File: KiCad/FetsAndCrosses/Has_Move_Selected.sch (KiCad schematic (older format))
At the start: 0 parts

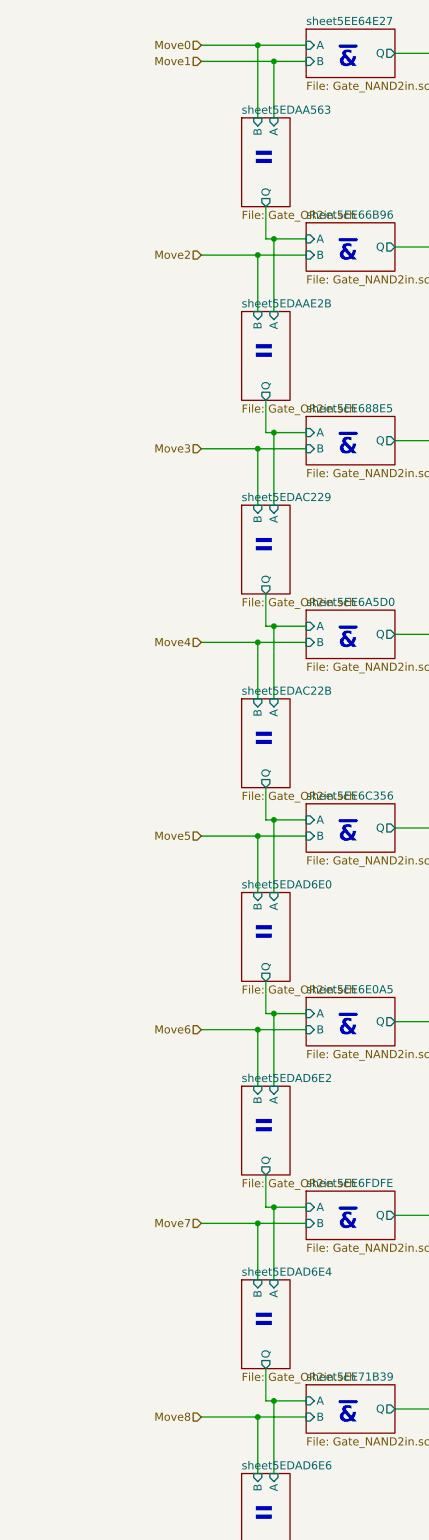
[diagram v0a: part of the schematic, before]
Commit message: Reworked everything to use Buses
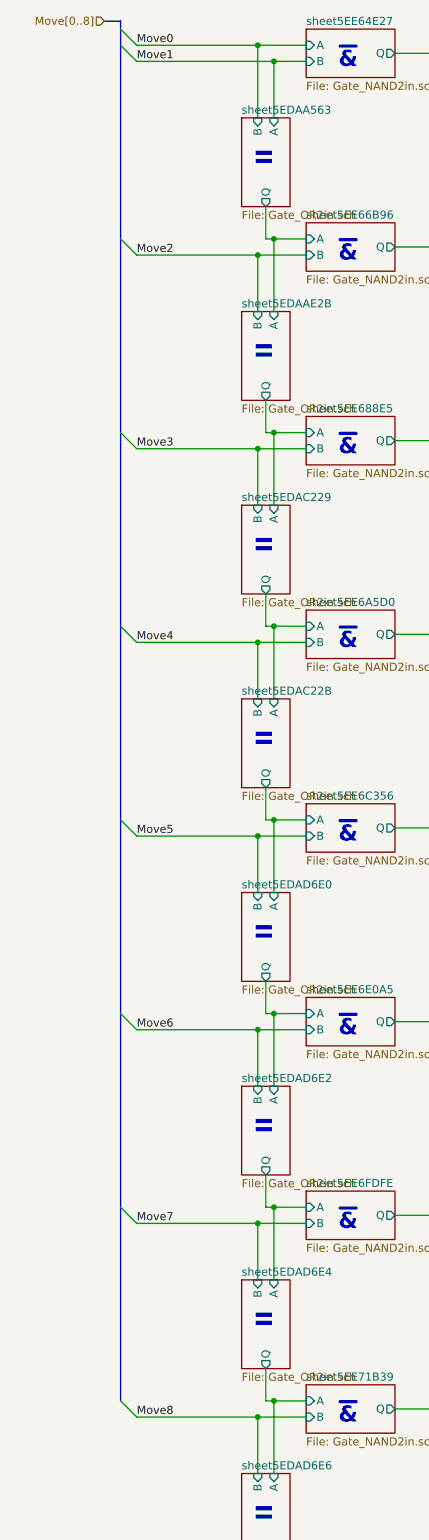
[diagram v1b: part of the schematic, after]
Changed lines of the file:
@@
 $Descr A4 8268 11693 portrait
 encoding utf-8
-Sheet 67 215
+Sheet 176 400
 Title ""
 Date ""
@@
 Comment4 ""
 $EndDescr
-Text HLabel 1700 800  0    50   Input ~ 0
-Move0
 Text Notes 2150 1450 3    100  ~ 20
 II
@@
 Wire Wire Line
 	2050 9300 2350 9300
-Wire Wire Line
-	2150 900  1700 900
 Connection ~ 2150 900
-Wire Wire Line
-	2050 800  1700 800
 Connection ~ 2050 800
-Wire Wire Line
-	1700 2100 2050 2100
-Wire Wire Line
-	1700 3300 2050 3300
-Wire Wire Line
-	1700 4500 2050 4500
-Wire Wire Line
-	1700 5700 2050 5700
-Wire Wire Line
-	1700 6900 2050 6900
-Wire Wire Line
-	1700 8100 2050 8100
-Wire Wire Line
-	1700 9300 2050 9300
-Text HLabel 1700 9300 0    50   Input ~ 0
-Move8
-Text HLabel 1700 8100 0    50   Input ~ 0
-Move7
-Text HLabel 1700 6900 0    50   Input ~ 0
-Move6
-Text HLabel 1700 5700 0    50   Input ~ 0
-Move5
-Text HLabel 1700 4500 0    50   Input ~ 0
-Move4
-Text HLabel 1700 3300 0    50   Input ~ 0
-Move3
-Text HLabel 1700 2100 0    50   Input ~ 0
-Move2
-Text HLabel 1700 900  0    50   Input ~ 0
-Move1
 $Sheet
 S 5550 1950 550  300
@@
 Text Notes 4700 2150 0    100  ~ 20
 &
+Entry Wire Line
+	1200 700  1300 800
+Entry Wire Line
+	1200 800  1300 900
+Entry Wire Line
+	1200 2000 1300 2100
+Entry Wire Line
+	1200 4400 1300 4500
+Entry Wire Line
+	1200 5600 1300 5700
+Entry Wire Line
+	1200 6800 1300 6900
+Entry Wire Line
+	1200 8000 1300 8100
+Entry Wire Line
+	1200 9200 1300 9300
+Wire Bus Line
+	1200 650  1100 650
+Text HLabel 1100 650  0    50   Input ~ 0
+Move[0..8]
+Text Label 1300 800  0    50   ~ 0
+Move0
+Text Label 1300 900  0    50   ~ 0
+Move1
+Text Label 1300 2100 0    50   ~ 0
+Move2
+Text Label 1300 4500 0    50   ~ 0
+Move4
+Text Label 1300 5700 0    50   ~ 0
+Move5
+Text Label 1300 6900 0    50   ~ 0
+Move6
+Text Label 1300 8100 0    50   ~ 0
+Move7
+Text Label 1300 9300 0    50   ~ 0
+Move8
+Text Label 1300 3300 0    50   ~ 0
+Move3
+Entry Wire Line
+	1200 3200 1300 3300
+Wire Wire Line
+	1300 9300 2050 9300
+Wire Wire Line
+	1300 8100 2050 8100
+Wire Wire Line
+	1300 6900 2050 6900
+Wire Wire Line
+	1300 5700 2050 5700
+Wire Wire Line
+	1300 4500 2050 4500
+Wire Wire Line
+	1300 3300 2050 3300
+Wire Wire Line
+	1300 2100 2050 2100
+Wire Wire Line
+	1300 800  2050 800
+Wire Wire Line
+	1300 900  2150 900
+Wire Bus Line
+	1200 650  1200 9200
 $EndSCHEMATC

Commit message: Schematic fixes.
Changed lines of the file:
@@
 Sheet 223 389
 Title ""
-Date ""
-Rev ""
-Comp ""
-Comment1 ""
+Date "2020-07-05"
+Rev "v0.0"
+Comp "Philipp Schilk"
+Comment1 "c"
 Comment2 ""
 Comment3 ""
@@
 Wire Wire Line
 	1300 900  2150 900
-Wire Bus Line
-	1200 650  1200 9200
 Entry Wire Line
 	1200 700  1300 800
@@
 Connection ~ 2150 900
 Connection ~ 2050 800
+Text Notes 5750 2200 0    100  ~ 20
+&
+Wire Bus Line
+	1200 650  1200 9200
 $EndSCHEMATC
